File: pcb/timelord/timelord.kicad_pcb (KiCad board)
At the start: 4 copper layers, 65 x 56 mm, 37 parts, among them J1 GPIO, J2 BCKP_PWR, J3 OLED, J4 EXTERNAL, J5 SMA, Q1 BC846, Q2 BC846, U2 NEO-F10T, U3 DS3231MZ

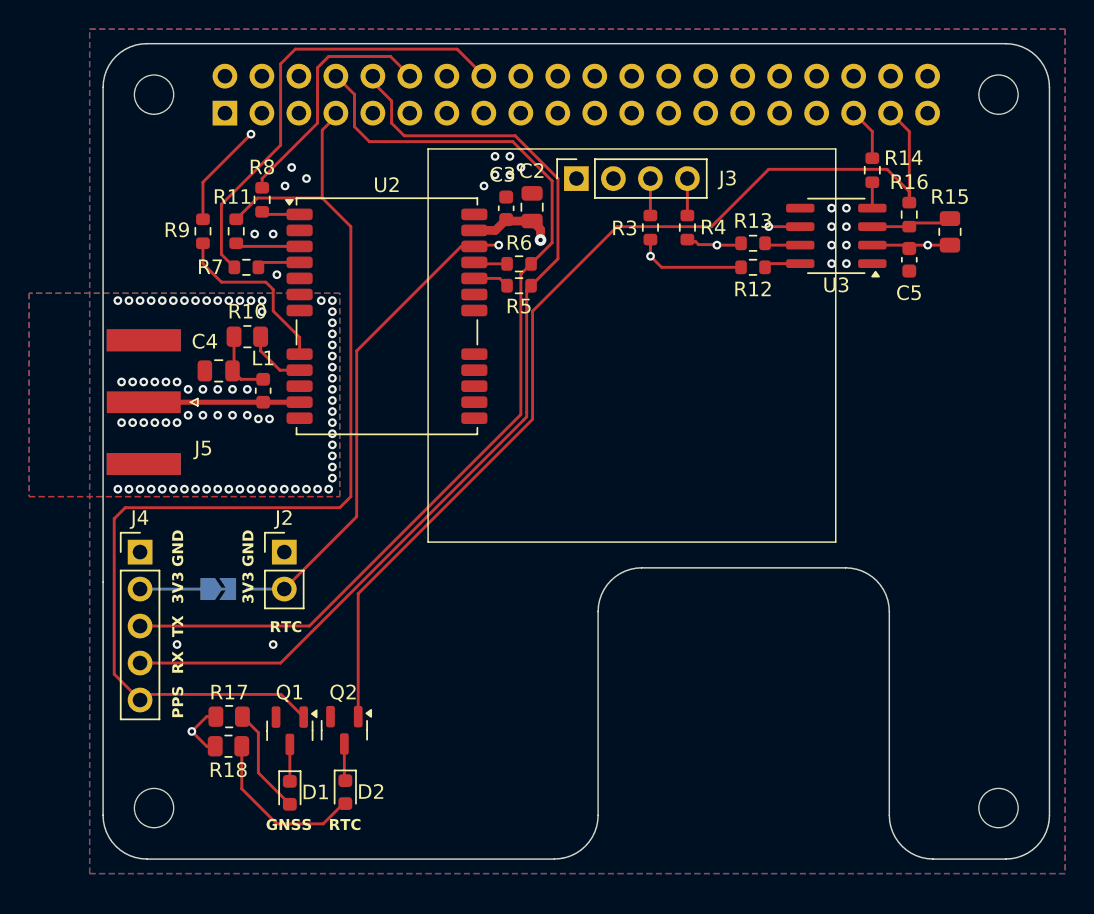
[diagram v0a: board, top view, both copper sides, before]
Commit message: Fix MFRs and component sizing
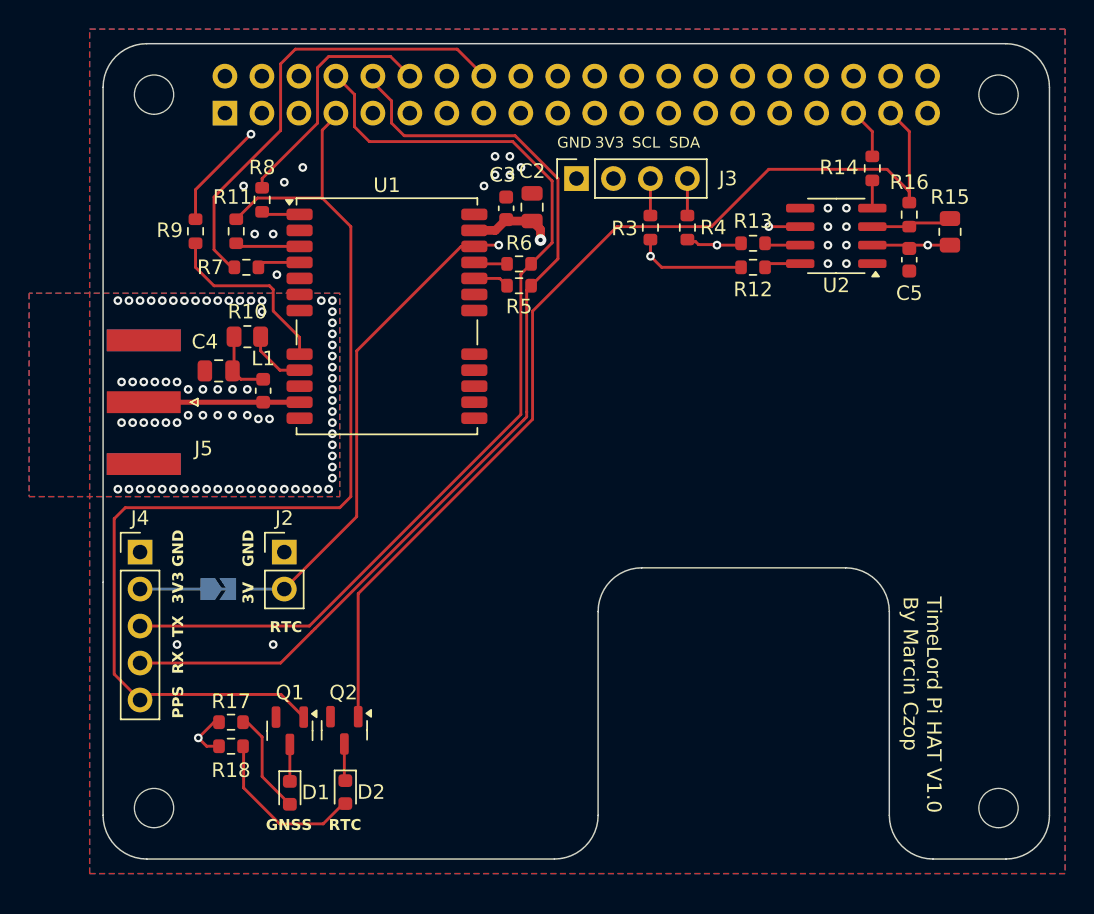
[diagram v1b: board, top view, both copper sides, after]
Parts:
- removed U3: DS3231MZ, Package_SO:SOIC-8_3.9x4.9mm_P1.27mm
- added U2: DS3232M, Package_SO:SOIC-8_3.9x4.9mm_P1.27mm, F.Cu at (150.4, 57.2)
- R17, R18: value 1k -> 470; footprint Resistor_SMD:R_0805_2012Metric -> Resistor_SMD:R_0603_1608Metric
- moved R9 0.51 mm to (106.3, 56.9)
- moved R17 0.40 mm to (108.8, 90.6)
- moved R18 0.17 mm to (108.8, 92.3)
- moved R14 0.13 mm to (152.8, 52.6)
- renumbered U2 to U1
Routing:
- net Net-(U1-~{RESET}): track 12.2 -> 12.8 mm
- net EXTINT: track 31.3 -> 31.9 mm
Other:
- board text added: "3V"
- board text added: "SCL"
- board text added: "SDA"
- board text added: "TimeLord Pi HAT V1.0 By Marcin Czop"

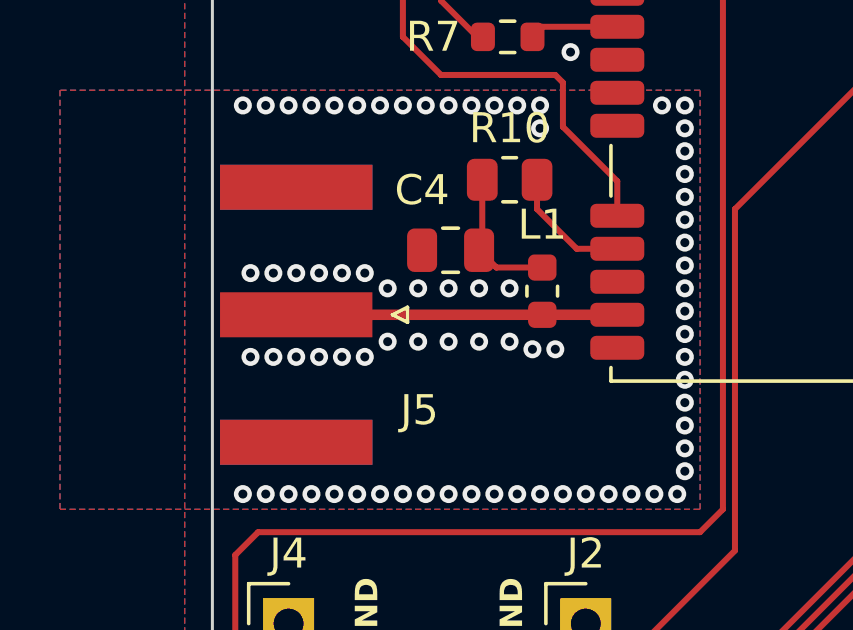
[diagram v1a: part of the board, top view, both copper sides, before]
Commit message: Reworked RF part of the PCB
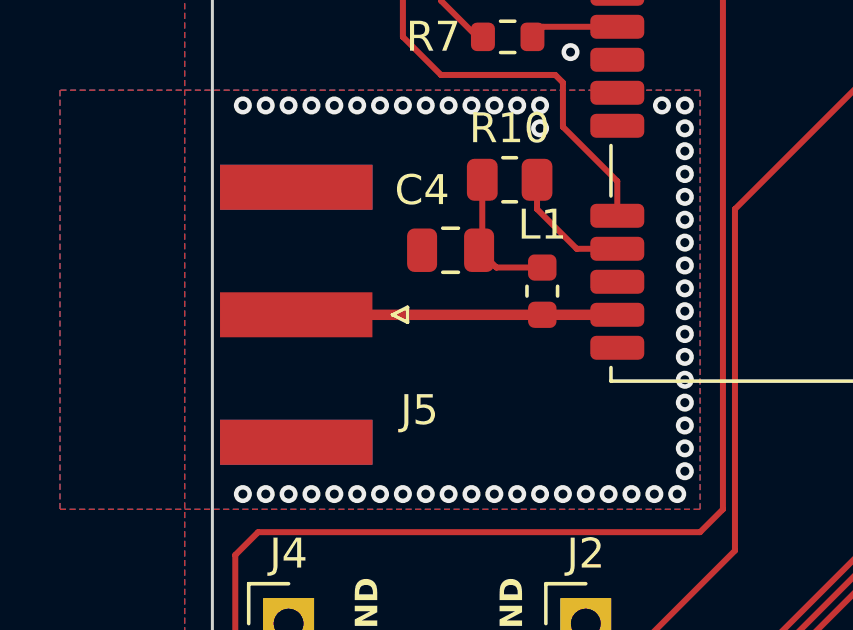
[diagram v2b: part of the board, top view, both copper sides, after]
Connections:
- net Net-(J5-In) renamed RF
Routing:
- net GND: vias 99 -> 75
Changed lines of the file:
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@@
 	(net 36 "Net-(J3-Pin_3)")
 	(net 37 "Net-(J3-Pin_4)")
-	(net 38 "Net-(J5-In)")
+	(net 38 "RF")
 	(net 39 "Net-(U1-TXD)")
 	(net 40 "Net-(U1-RXD)")
@@
 			(layers "F.Cu" "F.Mask" "F.Paste")
 			(roundrect_rratio 0.25)
-			(net 38 "Net-(J5-In)")
+			(net 38 "RF")
 			(pinfunction "RF_IN")
 			(pintype "input")
@@
 			(layers "F.Cu" "F.Mask" "F.Paste")
 			(roundrect_rratio 0.25)
-			(net 38 "Net-(J5-In)")
+			(net 38 "RF")
 			(pinfunction "2")
 			(pintype "passive")
@@
 			(size 1.5 5.08)
 			(layers "F.Cu" "F.Mask" "F.Paste")
-			(net 38 "Net-(J5-In)")
+			(net 38 "RF")
 			(pinfunction "In")
 			(pintype "passive")
@@
 	)
 	(via
-		(at 107.874 67.742)
-		(size 0.6)
-		(drill 0.3)
-		(layers "F.Cu" "B.Cu")
-		(free yes)
-		(net 1)
-	)
-	(via
-		(at 111.43 69.774)
-		(size 0.6)
-		(drill 0.3)
-		(layers "F.Cu" "B.Cu")
-		(free yes)
-		(net 1)
-	)
-	(via
 		(at 126.924 51.74)
 		(size 0.6)
@@
 	)
 	(via
-		(at 105.08 70.028)
-		(size 0.6)
-		(drill 0.3)
-		(layers "F.Cu" "B.Cu")
-		(free yes)
-		(net 1)
-	)
-	(via
 		(at 111.684 74.6)
 		(size 0.6)
@@
 	)
 	(via
-		(at 101.27 67.234)
-		(size 0.6)
-		(drill 0.3)
-		(layers "F.Cu" "B.Cu")
-		(free yes)
-		(net 1)
-	)
-	(via
-		(at 105.842 67.742)
-		(size 0.6)
-		(drill 0.3)
-		(layers "F.Cu" "B.Cu")
-		(free yes)
-		(net 1)
-	)
-	(via
-		(at 109.906 67.742)
-		(size 0.6)
-		(drill 0.3)
-		(layers "F.Cu" "B.Cu")
-		(free yes)
-		(net 1)
-	)
-	(via
 		(at 151.054 57.836)
 		(size 0.6)
@@
 	)
 	(via
-		(at 101.27 70.028)
-		(size 0.6)
-		(drill 0.3)
-		(layers "F.Cu" "B.Cu")
-		(free yes)
-		(net 1)
-	)
-	(via
 		(at 115.748 73.838)
 		(size 0.6)
@@
 	)
 	(via
-		(at 108.89 67.742)
-		(size 0.6)
-		(drill 0.3)
-		(layers "F.Cu" "B.Cu")
-		(free yes)
-		(net 1)
-	)
-	(via
 		(at 115.748 61.646)
 		(size 0.6)
@@
 	)
 	(via
-		(at 106.858 67.742)
-		(size 0.6)
-		(drill 0.3)
-		(layers "F.Cu" "B.Cu")
-		(free yes)
-		(net 1)
-	)
-	(via
 		(at 101.778 74.6)
 		(size 0.6)
@@
 	)
 	(via
-		(at 105.842 69.52)
-		(size 0.6)
-		(drill 0.3)
-		(layers "F.Cu" "B.Cu")
-		(free yes)
-		(net 1)
-	)
-	(via
-		(at 109.906 69.52)
-		(size 0.6)
-		(drill 0.3)
-		(layers "F.Cu" "B.Cu")
-		(free yes)
-		(net 1)
-	)
-	(via
 		(at 115.748 70.028)
 		(size 0.6)
@@
 	)
 	(via
-		(at 106.858 69.52)
-		(size 0.6)
-		(drill 0.3)
-		(layers "F.Cu" "B.Cu")
-		(free yes)
-		(net 1)
-	)
-	(via
 		(at 149.784 56.566)
 		(size 0.6)
@@
 	)
 	(via
-		(at 102.032 67.234)
-		(size 0.6)
-		(drill 0.3)
-		(layers "F.Cu" "B.Cu")
-		(free yes)
-		(net 1)
-	)
-	(via
 		(at 115.748 64.694)
 		(size 0.6)
@@
 	)
 	(via
-		(at 102.794 70.028)
-		(size 0.6)
-		(drill 0.3)
-		(layers "F.Cu" "B.Cu")
-		(free yes)
-		(net 1)
-	)
-	(via
 		(at 112.446 74.6)
 		(size 0.6)
@@
 	)
 	(via
-		(at 110.668 69.774)
-		(size 0.6)
-		(drill 0.3)
-		(layers "F.Cu" "B.Cu")
-		(free yes)
-		(net 1)
-	)
-	(via
 		(at 102.54 74.6)
 		(size 0.6)
@@
 	)
 	(via
-		(at 103.556 70.028)
-		(size 0.6)
-		(drill 0.3)
-		(layers "F.Cu" "B.Cu")
-		(free yes)
-		(net 1)
-	)
-	(via
 		(at 105.588 61.646)
 		(size 0.6)
@@
 	)
 	(via
-		(at 105.08 67.234)
-		(size 0.6)
-		(drill 0.3)
-		(layers "F.Cu" "B.Cu")
-		(free yes)
-		(net 1)
-	)
-	(via
 		(at 107.112 61.646)
 		(size 0.6)
@@
 	)
 	(via
-		(at 102.032 70.028)
-		(size 0.6)
-		(drill 0.3)
-		(layers "F.Cu" "B.Cu")
-		(free yes)
-		(net 1)
-	)
-	(via
 		(at 149.784 57.836)
 		(size 0.6)
@@
 	)
 	(via
-		(at 104.318 70.028)
-		(size 0.6)
-		(drill 0.3)
-		(layers "F.Cu" "B.Cu")
-		(free yes)
-		(net 1)
-	)
-	(via
 		(at 115.748 65.456)
 		(size 0.6)
@@
 	)
 	(via
-		(at 103.556 67.234)
-		(size 0.6)
-		(drill 0.3)
-		(layers "F.Cu" "B.Cu")
-		(free yes)
-		(net 1)
-	)
-	(via
 		(at 103.302 74.6)
 		(size 0.6)
@@
 	)
 	(via
-		(at 108.89 69.52)
-		(size 0.6)
-		(drill 0.3)
-		(layers "F.Cu" "B.Cu")
-		(free yes)
-		(net 1)
-	)
-	(via
 		(at 127.94 51.74)
 		(size 0.6)
@@
 	)
 	(via
-		(at 102.794 67.234)
-		(size 0.6)
-		(drill 0.3)
-		(layers "F.Cu" "B.Cu")
-		(free yes)
-		(net 1)
-	)
-	(via
-		(at 107.874 69.52)
-		(size 0.6)
-		(drill 0.3)
-		(layers "F.Cu" "B.Cu")
-		(free yes)
-		(net 1)
-	)
-	(via
 		(at 126.162 53.772)
 		(size 0.6)
@@
 	)
 	(via
-		(at 104.318 67.234)
-		(size 0.6)
-		(drill 0.3)
-		(layers "F.Cu" "B.Cu")
-		(free yes)
-		(net 1)
-	)
-	(via
 		(at 108.636 74.6)
 		(size 0.6)
@@
 	)
 	(segment
-		(start 102.496 68.624)
-		(end 110.996 68.624)
+		(start 110.996 68.624)
+		(end 102.794 68.624)
 		(width 0.3493)
 		(layer "F.Cu")

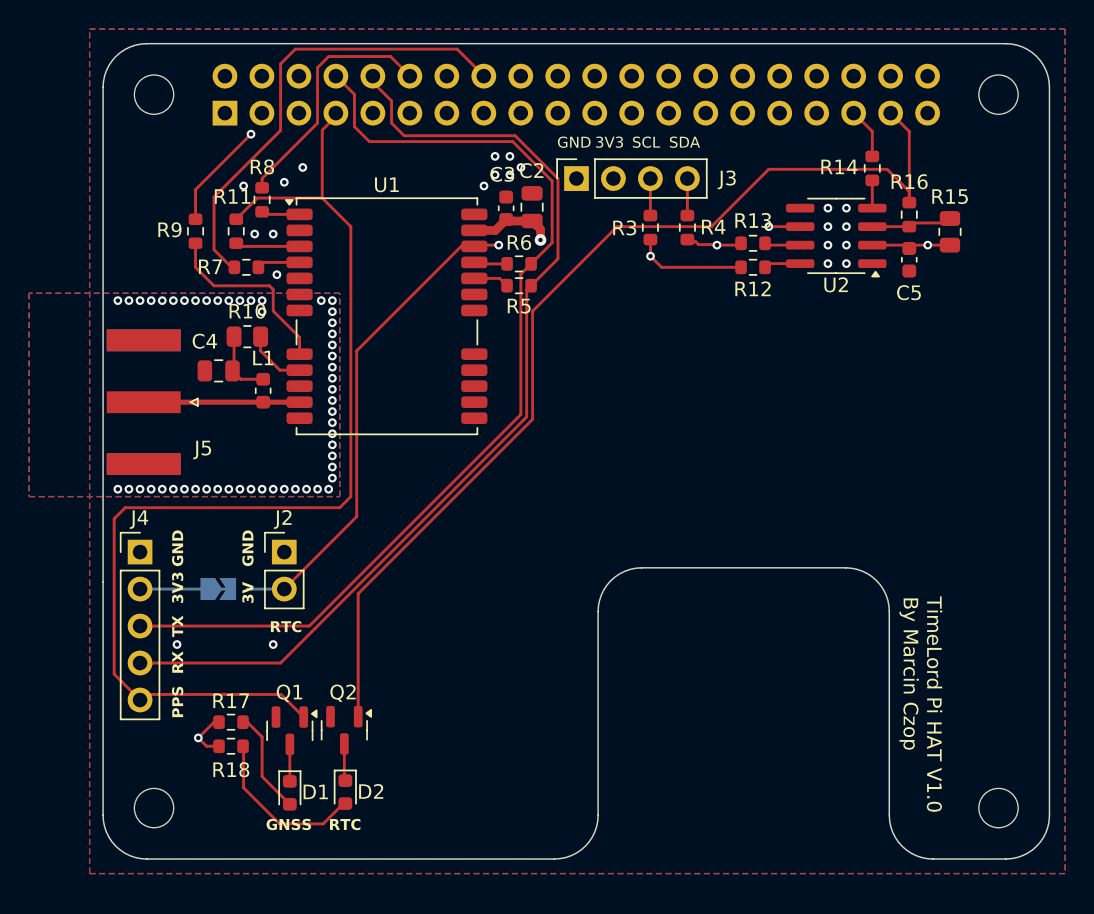
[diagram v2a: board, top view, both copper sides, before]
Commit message: Add SMA PPS connector and change 5V plane to GND plane
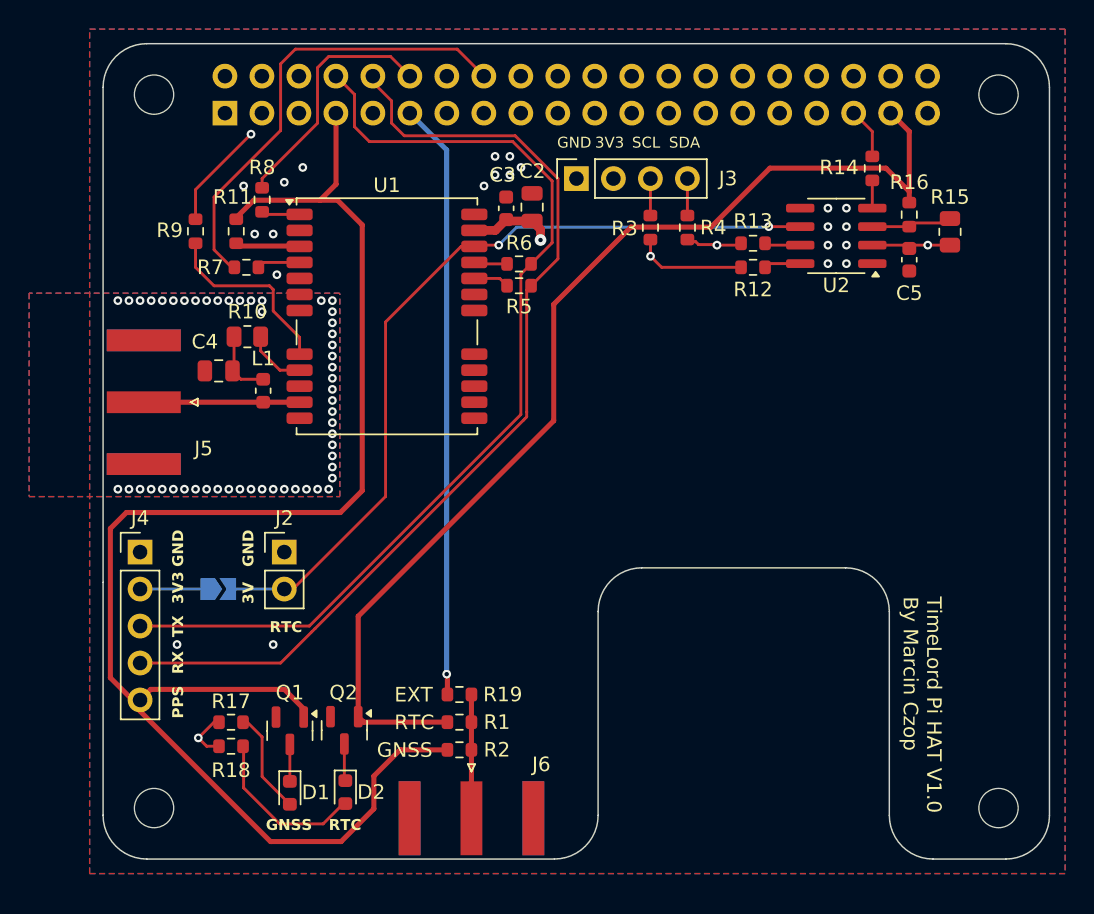
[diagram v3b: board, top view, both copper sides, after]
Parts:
- added J6: SMA, Connector_Coaxial:SMA_Amphenol_132289_EdgeMount, F.Cu at (125.3, 97.2)
- added R1: 0, Resistor_SMD:R_0603_1608Metric, F.Cu at (124.5, 90.6)
- added R19: 0, Resistor_SMD:R_0603_1608Metric, F.Cu at (124.5, 88.7)
- added R2: 0, Resistor_SMD:R_0603_1608Metric, F.Cu at (124.5, 92.5)
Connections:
- J1 pad 11: /GPIO17 -> PPS_EXT
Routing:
- net PPS_EXT: track 0.00 -> 41.0 mm, vias 0 -> 1
- net PPS: track 76.1 -> 108.3 mm
- net +3.3V: track 33.0 -> 19.4 mm
- net Net-(J6-In): track 0.00 -> 8.40 mm
- net PPS_RTC: track 70.6 -> 76.4 mm
- net VCC_BCKP: track 55.0 -> 56.6 mm
- removed copper zone on In1.Cu, net +5V
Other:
- board text added: "EXT"

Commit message: Changes
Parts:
- added J7: I2C pinout, Connector_PinSocket_2.54mm:PinSocket_1x04_P2.54mm_Vertical, F.Cu at (162.2, 66.0)
- added J8: UART3, Connector_PinHeader_2.54mm:PinHeader_1x03_P2.54mm_Vertical, F.Cu at (150.1, 66.0)
- added J9: UART4, Connector_PinHeader_2.54mm:PinHeader_1x03_P2.54mm_Vertical, F.Cu at (154.8, 66.0)
- added R20: 33, Resistor_SMD:R_0603_1608Metric, F.Cu at (158.7, 71.0)
- added R21: 33, Resistor_SMD:R_0603_1608Metric, F.Cu at (158.7, 73.5)
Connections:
- net /GPIO10/SPI0.MOSI renamed /GPIO10
- net /GPIO11/SPI0.SCLK renamed /GPIO11
- net /GPIO7/SPI0.CE1 renamed /GPIO7
- net UART_RX renamed UART0_RX
- net UART_TX renamed UART0_TX
- J1 pad 21: /GPIO9/SPI0.MISO -> UART3_RX
- J1 pad 24: /GPIO8/SPI0.CE0 -> UART3_TX
- J1 pad 32: /GPIO12/PWM0 -> UART4_TX
- J1 pad 33: /GPIO13/PWM1 -> UART4_RX
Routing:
- net UART3_RX: track 0.00 -> 41.5 mm
- net UART3_TX: track 0.00 -> 33.0 mm
- net UART4_TX: track 0.00 -> 28.3 mm
- net SDA: track 40.6 -> 67.7 mm
- net SCL: track 37.0 -> 59.3 mm
- net UART4_RX: track 0.00 -> 22.1 mm
- net Net-(J7-Pin_4): track 0.00 -> 2.78 mm
- net Net-(J7-Pin_3): track 0.00 -> 2.77 mm
- net +5V: track 0.00 -> 2.54 mm
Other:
- board text added: "U3"
- board text added: "U4"
